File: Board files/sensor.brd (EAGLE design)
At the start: 25.4 x 59.7 mm, 33 parts, among them Q1 BCM847DS, U1 TL974, U2 TL974

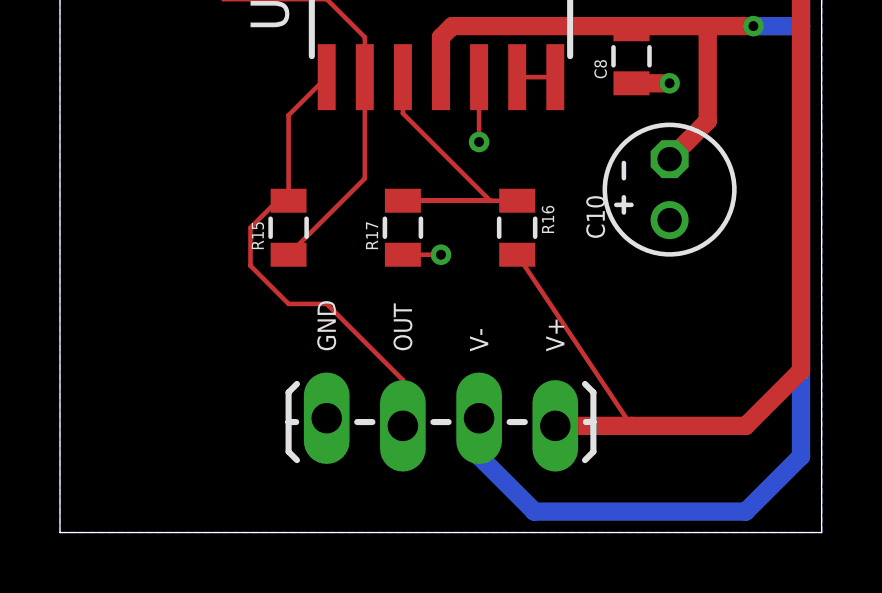
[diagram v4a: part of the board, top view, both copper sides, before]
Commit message: Changed logic board layout
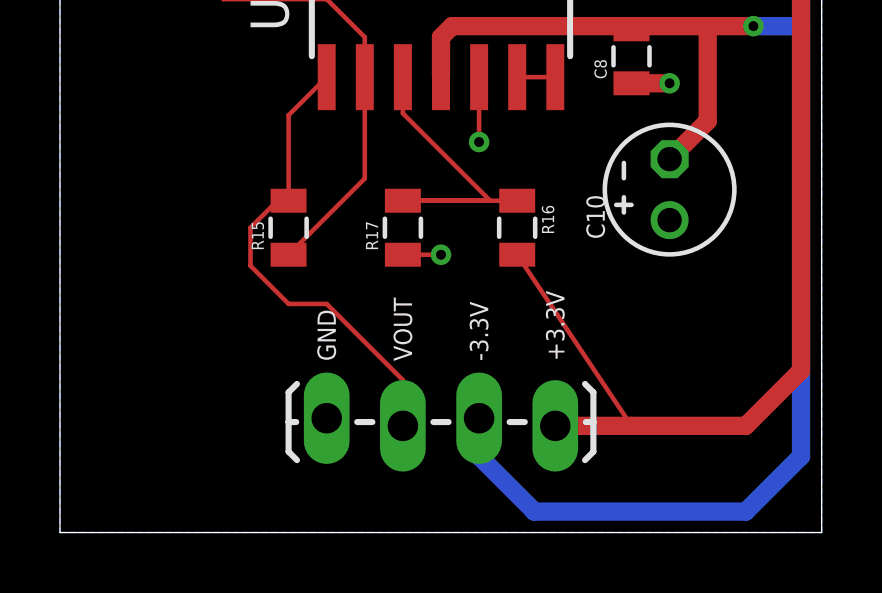
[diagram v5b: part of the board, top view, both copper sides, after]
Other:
- board text added: "+3.3V"
- board text added: "-3.3V"
- board text added: "VOUT"
- board text removed: "OUT"
- board text removed: "V+"
- board text removed: "V-"
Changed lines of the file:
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@@
 <wire x1="25.3875" y1="59.68" x2="0" y2="59.68" width="0" layer="20"/>
 <wire x1="0" y1="59.68" x2="0" y2="0" width="0" layer="20"/>
-<text x="8.89" y="6.0325" size="0.6096" layer="21" rot="R270" align="center-right">GND</text>
-<text x="11.43" y="6.0325" size="0.6096" layer="21" rot="R270" align="center-right">OUT</text>
-<text x="13.97" y="6.0325" size="0.6096" layer="21" rot="R270" align="center-right">V-</text>
-<text x="16.51" y="6.0325" size="0.6096" layer="21" rot="R270" align="center-right">V+</text>
+<text x="8.89" y="5.715" size="0.6096" layer="21" rot="R270" align="center-right">GND</text>
+<text x="11.43" y="5.715" size="0.6096" layer="21" rot="R270" align="center-right">VOUT</text>
+<text x="13.97" y="5.715" size="0.6096" layer="21" rot="R270" align="center-right">-3.3V</text>
+<text x="16.51" y="5.715" size="0.6096" layer="21" rot="R270" align="center-right">+3.3V</text>
 </plain>
 <attributes>

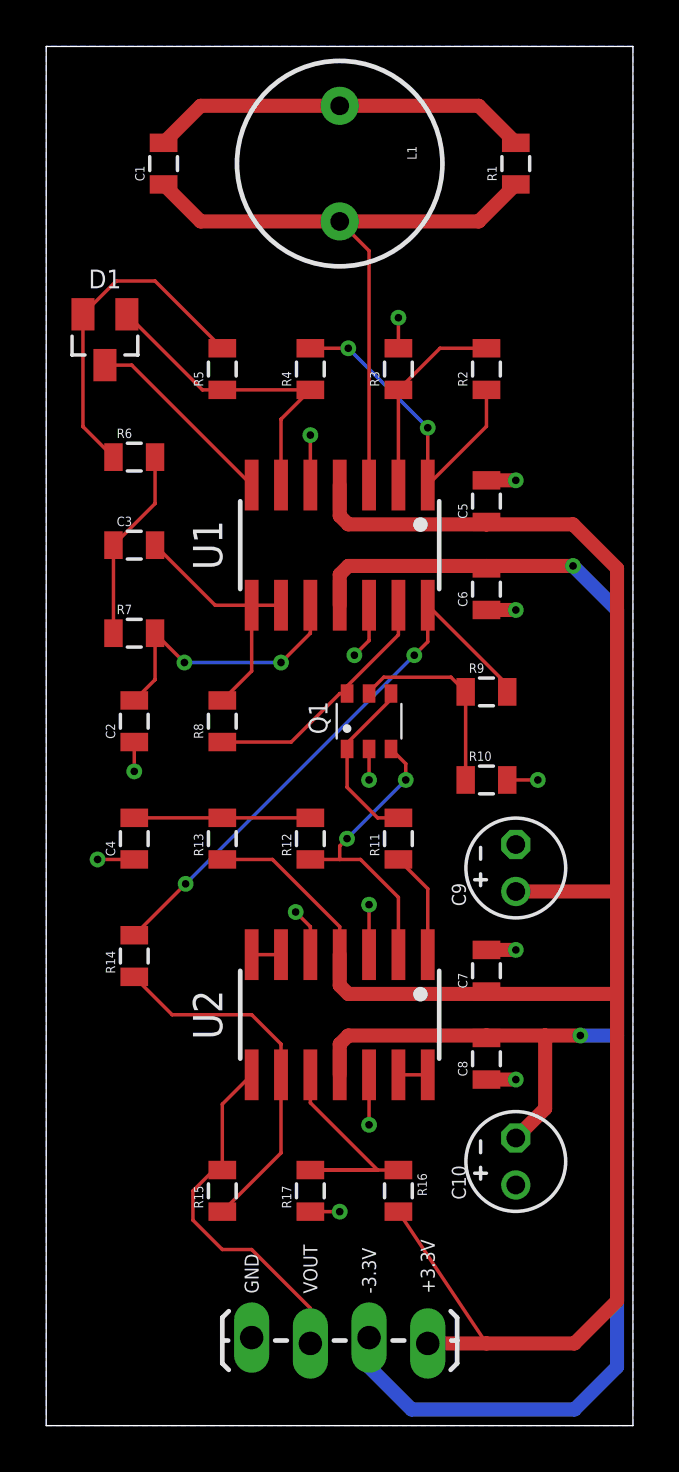
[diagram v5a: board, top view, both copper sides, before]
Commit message: Switched to polarized connectors
Also added 3.3v out pins on logic board, various other changes
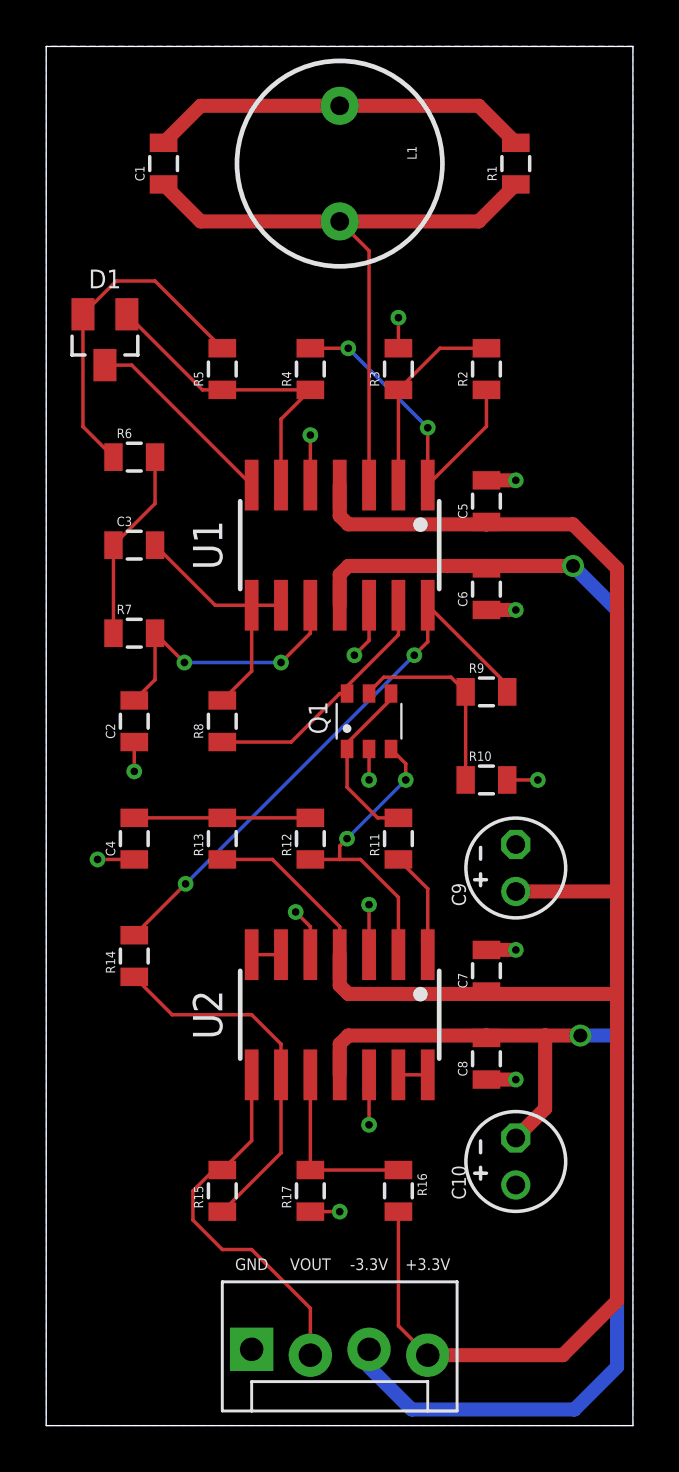
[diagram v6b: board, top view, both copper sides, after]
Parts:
- JP1: device SparkFun-Connectors:1X04_LOCK_LONGPADS -> SparkFun-Connectors:MOLEX-1X4_LOCK
- moved JP1 0.64 mm to (8.89, 3.17)
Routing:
- net N$20: track 12.0 -> 7.93 mm
- net N$24: track 15.7 -> 16.2 mm
- net VNEG: track 79.2 -> 78.7 mm
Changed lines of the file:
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@@
 <wire x1="25.3875" y1="59.68" x2="0" y2="59.68" width="0" layer="20"/>
 <wire x1="0" y1="59.68" x2="0" y2="0" width="0" layer="20"/>
-<text x="8.89" y="5.715" size="0.6096" layer="21" rot="R270" align="center-right">GND</text>
-<text x="11.43" y="5.715" size="0.6096" layer="21" rot="R270" align="center-right">VOUT</text>
-<text x="13.97" y="5.715" size="0.6096" layer="21" rot="R270" align="center-right">-3.3V</text>
-<text x="16.51" y="5.715" size="0.6096" layer="21" rot="R270" align="center-right">+3.3V</text>
+<text x="8.89" y="6.985" size="0.508" layer="21" align="center">GND</text>
+<text x="11.43" y="6.985" size="0.508" layer="21" align="center">VOUT</text>
+<text x="13.97" y="6.985" size="0.508" layer="21" align="center">-3.3V</text>
+<text x="16.51" y="6.985" size="0.508" layer="21" align="center">+3.3V</text>
 </plain>
 <attributes>
@@
 </autorouter>
 <elements>
-<element name="JP1" library="SparkFun-Connectors" package="1X04_LOCK_LONGPADS" value="" x="8.89" y="3.81" smashed="yes">
-<attribute name="VALUE" x="7.62" y="0.508" size="1.27" layer="27" font="vector"/>
+<element name="JP1" library="SparkFun-Connectors" package="MOLEX-1X4_LOCK" value="" x="8.89" y="3.175" smashed="yes">
+<attribute name="VALUE" x="7.62" y="-0.127" size="1.27" layer="27" font="vector"/>
 </element>
 <element name="L1" library="SparkFun-Passives" package="RLB0912" value="1mH" x="12.7" y="54.61" rot="R270"/>
@@
 <contactref element="U1" pad="4"/>
 <contactref element="U2" pad="4"/>
-<wire x1="16.51" y1="3.556" x2="19.05" y2="3.556" width="0.6096" layer="1"/>
-<wire x1="19.05" y1="3.556" x2="22.86" y2="3.556" width="0.6096" layer="1"/>
-<wire x1="22.86" y1="3.556" x2="24.7015" y2="5.3975" width="0.6096" layer="1"/>
+<wire x1="22.352" y1="3.048" x2="24.7015" y2="5.3975" width="0.6096" layer="1"/>
 <wire x1="24.7015" y1="5.3975" x2="24.7015" y2="18.68" width="0.6096" layer="1"/>
-<wire x1="24.7015" y1="18.68" x2="24.7015" y2="22.86" width="0.6096" layer="1"/>
+<wire x1="24.7015" y1="18.68" x2="24.7015" y2="23.114" width="0.6096" layer="1"/>
 <wire x1="24.7015" y1="23.114" x2="24.7015" y2="37.095" width="0.6096" layer="1"/>
 <wire x1="24.7015" y1="37.095" x2="22.7965" y2="39" width="0.6096" layer="1"/>
@@
 <wire x1="13.07" y1="39" x2="12.7" y2="39.37" width="0.6096" layer="1"/>
 <wire x1="12.7" y1="39.37" x2="12.7" y2="40.7" width="0.6096" layer="1"/>
-<wire x1="15.24" y1="9.26" x2="19.05" y2="3.556" width="0.1524" layer="1"/>
 <contactref element="C5" pad="1"/>
 <contactref element="C7" pad="1"/>
@@
 <contactref element="C9" pad="+"/>
 <wire x1="20.32" y1="23.114" x2="24.7015" y2="23.114" width="0.6096" layer="1"/>
-<wire x1="24.7015" y1="23.114" x2="24.7015" y2="22.86" width="0.6096" layer="1"/>
+<wire x1="16.51" y1="3.048" x2="22.352" y2="3.048" width="0.6096" layer="1"/>
+<wire x1="15.24" y1="9.26" x2="15.24" y2="4.318" width="0.1524" layer="1"/>
+<wire x1="15.24" y1="4.318" x2="16.51" y2="3.048" width="0.1524" layer="1"/>
 </signal>
 <signal name="N$3">
@@
 <contactref element="U1" pad="11"/>
 <contactref element="U2" pad="11"/>
-<wire x1="13.97" y1="3.81" x2="13.97" y2="2.54" width="0.6096" layer="16"/>
 <wire x1="13.97" y1="2.54" x2="15.8115" y2="0.6985" width="0.6096" layer="16"/>
 <wire x1="15.8115" y1="0.6985" x2="22.86" y2="0.6985" width="0.6096" layer="16"/>
@@
 <wire x1="24.7015" y1="2.54" x2="24.7015" y2="16.88" width="0.6096" layer="16"/>
 <wire x1="24.7015" y1="16.88" x2="24.7015" y2="35.295" width="0.6096" layer="16"/>
-<via x="23.114" y="16.88" extent="1-16" drill="0.3302"/>
-<wire x1="23.114" y1="16.88" x2="24.7015" y2="16.88" width="0.6096" layer="16"/>
-<via x="22.7965" y="37.2" extent="1-16" drill="0.3302"/>
-<wire x1="22.7965" y1="37.2" x2="24.7015" y2="35.295" width="0.6096" layer="16"/>
 <wire x1="13.07" y1="16.88" x2="12.7" y2="16.51" width="0.6096" layer="1"/>
 <wire x1="12.7" y1="16.51" x2="12.7" y2="15.18" width="0.6096" layer="1"/>
@@
 <wire x1="21.59" y1="13.716" x2="21.59" y2="16.88" width="0.6096" layer="1"/>
 <wire x1="20.32" y1="12.446" x2="21.59" y2="13.716" width="0.6096" layer="1"/>
+<via x="22.7965" y="37.2" extent="1-16" drill="0.6"/>
+<wire x1="22.7965" y1="37.2" x2="24.7015" y2="35.295" width="0.6096" layer="16"/>
+<via x="23.114" y="16.88" extent="1-16" drill="0.6"/>
+<wire x1="23.114" y1="16.88" x2="24.7015" y2="16.88" width="0.6096" layer="16"/>
+<wire x1="13.97" y1="3.302" x2="13.97" y2="2.54" width="0.6096" layer="16"/>
 </signal>
 <signal name="N$2">
@@
 <contactref element="R17" pad="2"/>
 <contactref element="R16" pad="1"/>
-<wire x1="11.43" y1="15.18" x2="11.43" y2="13.97" width="0.1524" layer="1"/>
-<wire x1="11.43" y1="13.97" x2="14.34" y2="11.06" width="0.1524" layer="1"/>
-<wire x1="14.34" y1="11.06" x2="11.43" y2="11.06" width="0.1524" layer="1"/>
 <wire x1="11.43" y1="11.06" x2="15.24" y2="11.06" width="0.1524" layer="1"/>
+<wire x1="11.43" y1="15.18" x2="11.43" y2="11.06" width="0.1524" layer="1"/>
 </signal>
 <signal name="N$22">
@@
 <contactref element="R15" pad="2"/>
 <contactref element="JP1" pad="2"/>
-<wire x1="8.89" y1="15.18" x2="7.62" y2="13.91" width="0.1524" layer="1"/>
-<wire x1="7.62" y1="13.91" x2="7.62" y2="11.06" width="0.1524" layer="1"/>
 <wire x1="7.62" y1="11.06" x2="7.25" y2="11.06" width="0.1524" layer="1"/>
 <wire x1="7.25" y1="11.06" x2="6.35" y2="10.16" width="0.1524" layer="1"/>
@@
 <wire x1="7.62" y1="7.62" x2="8.89" y2="7.62" width="0.1524" layer="1"/>
 <wire x1="8.89" y1="7.62" x2="11.43" y2="5.08" width="0.1524" layer="1"/>
-<wire x1="11.43" y1="5.08" x2="11.43" y2="3.556" width="0.1524" layer="1"/>
+<wire x1="11.43" y1="5.08" x2="11.43" y2="3.048" width="0.1524" layer="1"/>
+<wire x1="8.89" y1="15.18" x2="8.89" y2="12.33" width="0.1524" layer="1"/>
+<wire x1="8.89" y1="12.33" x2="7.62" y2="11.06" width="0.1524" layer="1"/>
 </signal>
 <signal name="N$9">

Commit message: Modified boards to facilitate mounting
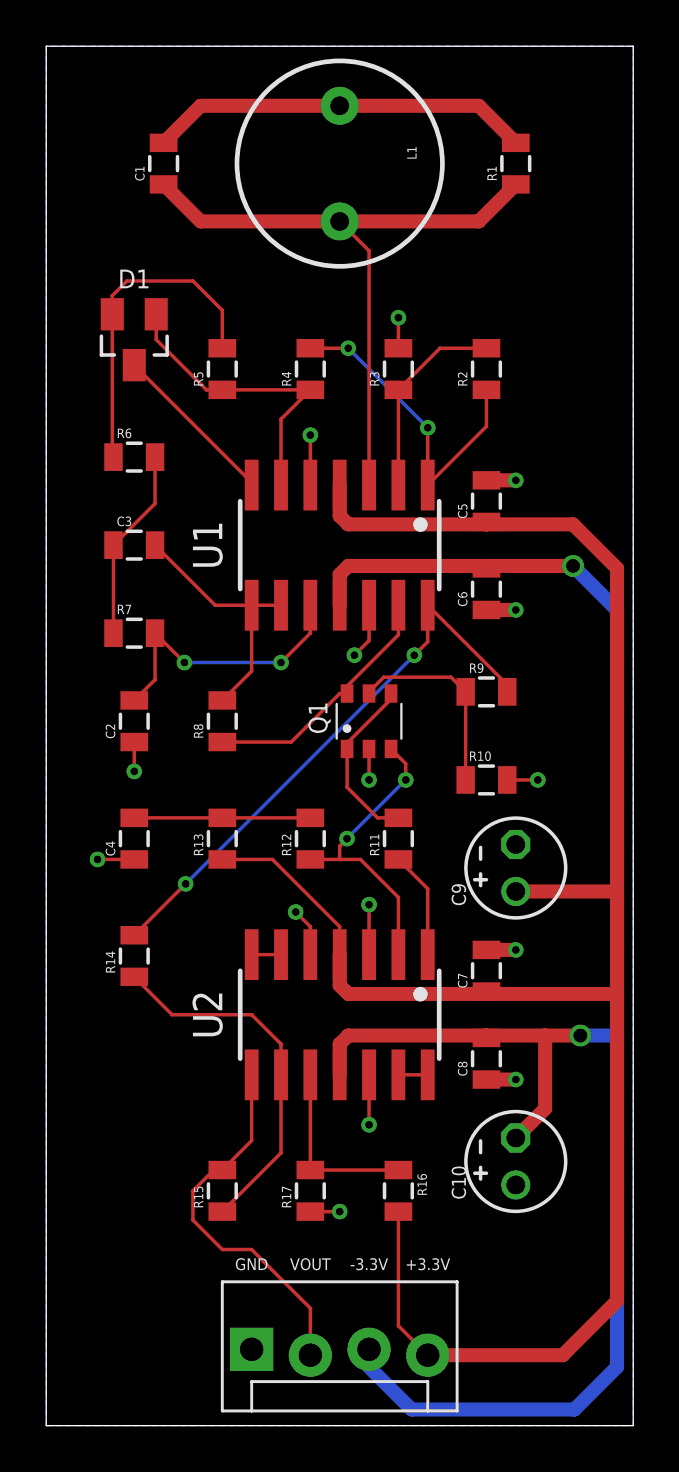
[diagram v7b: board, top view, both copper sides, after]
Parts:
- moved D1 1.27 mm to (3.81, 47.0)
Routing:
- net N$8: track 8.50 -> 7.40 mm
- net N$2: track 13.9 -> 13.3 mm
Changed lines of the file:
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@@
 <board>
 <plain>
-<wire x1="0" y1="0" x2="25.3875" y2="0" width="0" layer="20"/>
-<wire x1="25.3875" y1="0" x2="25.3875" y2="59.68" width="0" layer="20"/>
-<wire x1="25.3875" y1="59.68" x2="0" y2="59.68" width="0" layer="20"/>
-<wire x1="0" y1="59.68" x2="0" y2="0" width="0" layer="20"/>
+<wire x1="0" y1="0" x2="25.4" y2="0" width="0" layer="20"/>
+<wire x1="25.4" y1="0" x2="25.4" y2="59.69" width="0" layer="20"/>
+<wire x1="25.4" y1="59.69" x2="0" y2="59.69" width="0" layer="20"/>
+<wire x1="0" y1="59.69" x2="0" y2="0" width="0" layer="20"/>
 <text x="8.89" y="6.985" size="0.508" layer="21" align="center">GND</text>
 <text x="11.43" y="6.985" size="0.508" layer="21" align="center">VOUT</text>
@@
 <element name="C3" library="SparkFun-Capacitors" package="0805" value="0.22uF" x="3.81" y="38.1"/>
 <element name="R7" library="SparkFun-Resistors" package="0805" value="20K" x="3.81" y="34.29"/>
-<element name="D1" library="diode" package="SOT23" value="BAS70-04" x="2.54" y="46.99" smashed="yes" rot="R180">
-<attribute name="NAME" x="2.54" y="49.2125" size="0.8128" layer="25" rot="R180" align="top-center"/>
-<attribute name="VALUE" x="4.445" y="50.165" size="1.27" layer="27" rot="R180"/>
+<element name="D1" library="diode" package="SOT23" value="BAS70-04" x="3.81" y="46.99" smashed="yes" rot="R180">
+<attribute name="NAME" x="3.81" y="49.2125" size="0.8128" layer="25" rot="R180" align="top-center"/>
+<attribute name="VALUE" x="5.715" y="50.165" size="1.27" layer="27" rot="R180"/>
 </element>
 <element name="Q1" library="Custom" package="SOT-457" value="BCM847DS" x="13.97" y="30.48" smashed="yes">
@@
 <wire x1="10.16" y1="43.55" x2="11.43" y2="44.82" width="0.1524" layer="1"/>
 <wire x1="11.43" y1="44.82" x2="7.62" y2="44.82" width="0.1524" layer="1"/>
-<wire x1="7.62" y1="44.82" x2="6.76" y2="44.82" width="0.1524" layer="1"/>
-<wire x1="6.76" y1="44.82" x2="3.49" y2="48.09" width="0.1524" layer="1"/>
+<wire x1="7.62" y1="44.82" x2="6.9325" y2="44.82" width="0.1524" layer="1"/>
+<wire x1="6.9325" y1="44.82" x2="4.76" y2="46.9925" width="0.1524" layer="1"/>
+<wire x1="4.76" y1="46.9925" x2="4.76" y2="48.09" width="0.1524" layer="1"/>
 </signal>
 <signal name="N$5">
@@
 <contactref element="R5" pad="2"/>
 <contactref element="R6" pad="1"/>
-<wire x1="7.62" y1="46.62" x2="4.71" y2="49.53" width="0.1524" layer="1"/>
-<wire x1="4.71" y1="49.53" x2="3.03" y2="49.53" width="0.1524" layer="1"/>
-<wire x1="3.03" y1="49.53" x2="1.59" y2="48.09" width="0.1524" layer="1"/>
-<wire x1="1.59" y1="48.09" x2="1.59" y2="43.23" width="0.1524" layer="1"/>
-<wire x1="1.59" y1="43.23" x2="2.91" y2="41.91" width="0.1524" layer="1"/>
+<wire x1="2.86" y1="48.09" x2="2.86" y2="41.96" width="0.1524" layer="1"/>
+<wire x1="2.86" y1="41.96" x2="2.91" y2="41.91" width="0.1524" layer="1"/>
+<wire x1="7.62" y1="46.62" x2="7.62" y2="48.26" width="0.1524" layer="1"/>
+<wire x1="7.62" y1="48.26" x2="6.35" y2="49.53" width="0.1524" layer="1"/>
+<wire x1="6.35" y1="49.53" x2="3.4925" y2="49.53" width="0.1524" layer="1"/>
+<wire x1="3.4925" y1="49.53" x2="2.8575" y2="48.895" width="0.1524" layer="1"/>
+<wire x1="2.8575" y1="48.895" x2="2.8575" y2="48.0925" width="0.1524" layer="1"/>
+<wire x1="2.8575" y1="48.0925" x2="2.86" y2="48.09" width="0.1524" layer="1"/>
 </signal>
 <signal name="N$8">
 <contactref element="D1" pad="3"/>
 <contactref element="U1" pad="7"/>
-<wire x1="2.54" y1="45.89" x2="3.7" y2="45.89" width="0.1524" layer="1"/>
-<wire x1="3.7" y1="45.89" x2="8.89" y2="40.7" width="0.1524" layer="1"/>
+<wire x1="3.81" y1="45.89" x2="3.7" y2="45.89" width="0.1524" layer="1"/>
+<wire x1="8.89" y1="40.7" x2="8.89" y2="40.81" width="0.1524" layer="1"/>
+<wire x1="8.89" y1="40.81" x2="3.81" y2="45.89" width="0.1524" layer="1"/>
 </signal>
 <signal name="N$6">

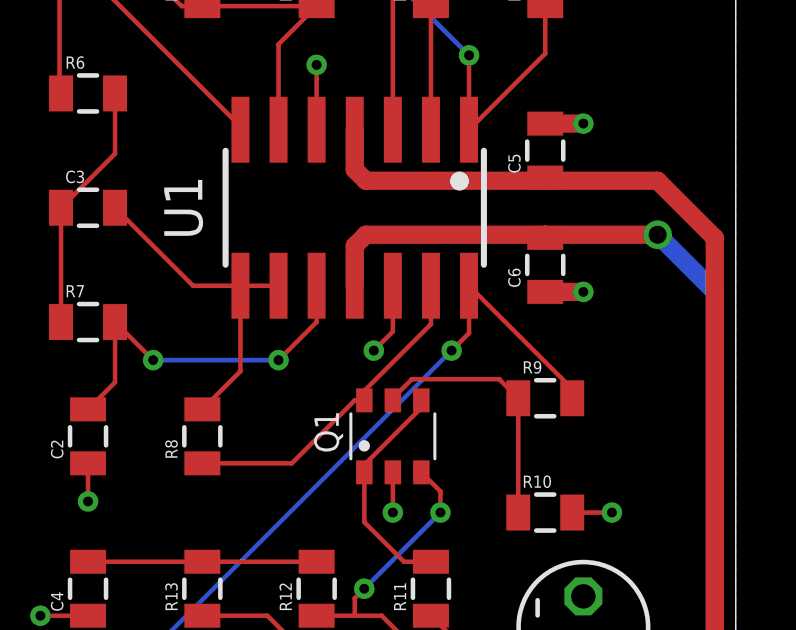
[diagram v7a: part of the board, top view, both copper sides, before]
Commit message: Fixed sensor board bug
Added a capacitor between U1p13 and U1p14
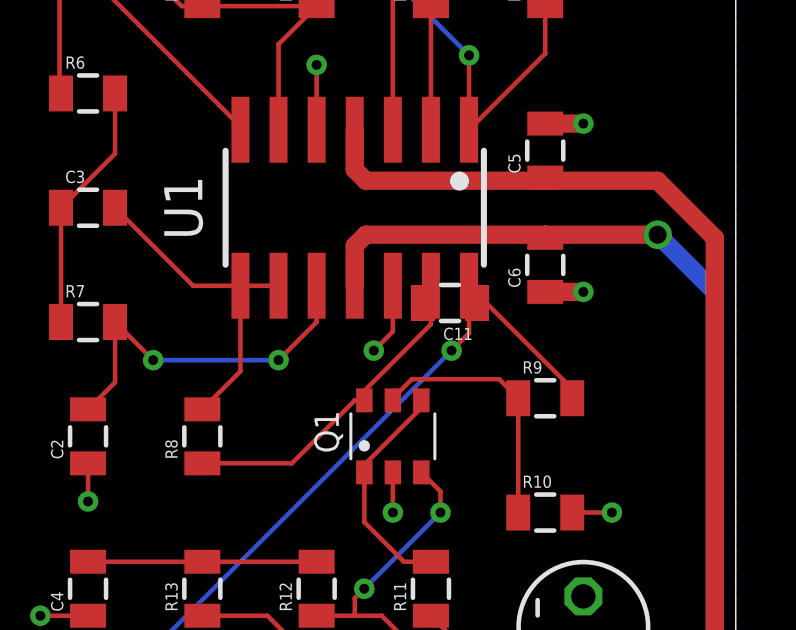
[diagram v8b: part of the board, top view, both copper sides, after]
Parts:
- added C11: 0.1uF, SparkFun-Capacitors:0805
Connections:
- net N$13: now also C11.2
- net N$17: now also C11.1
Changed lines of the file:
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@@
 <attribute name="VALUE" x="22.479" y="13.589" size="1.27" layer="27" ratio="10" rot="R90"/>
 </element>
+<element name="C11" library="SparkFun-Capacitors" package="0805" value="0.1uF" x="15.875" y="34.925" rot="R180"/>
 </elements>
 <signals>
@@
 <wire x1="10.6025" y1="29.58" x2="12.7025" y2="31.68" width="0.1524" layer="1"/>
 <wire x1="12.7025" y1="31.68" x2="13.02" y2="31.68" width="0.1524" layer="1"/>
+<contactref element="C11" pad="2"/>
+<wire x1="15.24" y1="35.5" x2="14.975" y2="34.925" width="0" layer="19" extent="1-1"/>
 </signal>
 <signal name="N$15">
@@
 <via x="6.0325" y="23.4425" extent="1-16" drill="0.3302"/>
 <wire x1="6.0325" y1="23.4425" x2="3.81" y2="21.22" width="0.1524" layer="1"/>
+<contactref element="C11" pad="1"/>
+<wire x1="16.51" y1="35.5" x2="16.775" y2="34.925" width="0" layer="19" extent="1-1"/>
 </signal>
 <signal name="N$19">
